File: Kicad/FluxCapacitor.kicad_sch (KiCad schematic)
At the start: 67 parts, among them J1 Jack-DC, J10 RELAY, J19 Conn_01x03_Socket, J2 TM_1, J20 Conn_01x03_Socket, J21 Conn_01x03_Socket, J22 Conn_01x03_Socket, J23 Conn_01x03_Socket, J3 TM_2, J4 Conn_01x02, J7 TM_1, J8 TM_1, J9 RELAY, K1 G5V-1, Q1 2N7000, Q2 IRF4905PBF, SW1 SW_SPDT_321, U1 OKI-78SR-5_1.5-W36-C, U2 ESP32_DEVBOARD

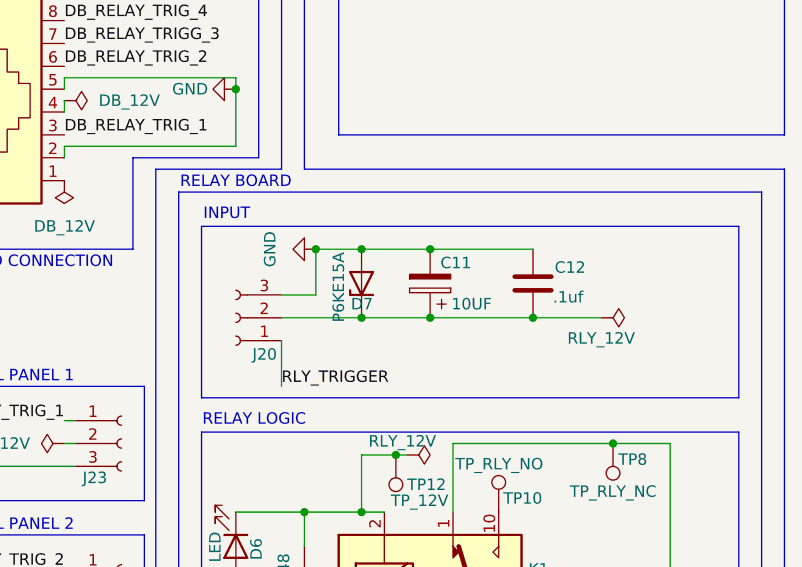
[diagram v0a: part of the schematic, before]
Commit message: File organization and power input work
-Changed file structure to make space for fusion files and firmware in one github repo.
-updated gitignore to account for fusion.
-added a mosfet for reverse polarity protection.
-changed electrolytic caps to polarized. -Created a flux capacitor library stored in the repo so that symbols aren't dependent on my personal library
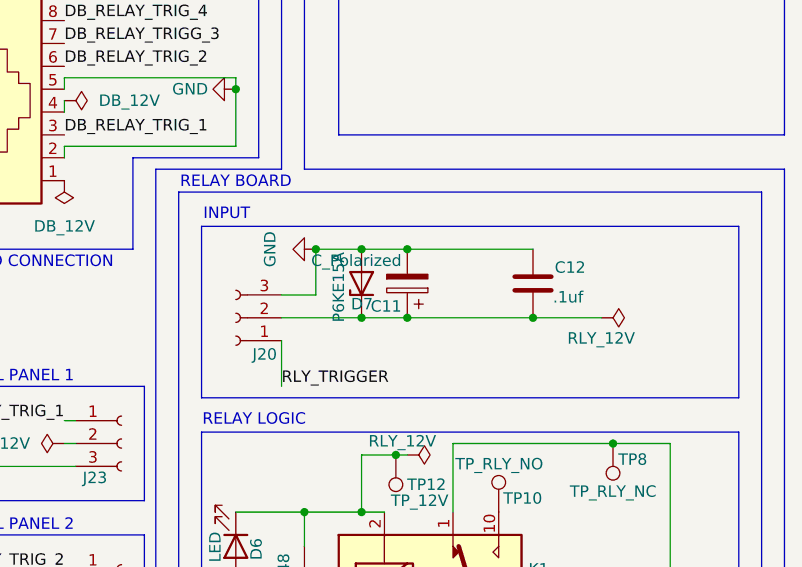
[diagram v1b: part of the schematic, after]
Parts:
- C11: value 10UF -> C_Polarized
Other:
- moved on the sheet: C11
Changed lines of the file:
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@@
 	)
 	(junction
-		(at 132.08 88.9)
+		(at 238.76 87.63)
 		(diameter 0)
 		(color 0 0 0 0)
 	)
 	(junction
-		(at 38.1 76.2)
+		(at 132.08 88.9)
 		(diameter 0)
 		(color 0 0 0 0)
 	)
 	(junction
-		(at 160.02 88.9)
+		(at 38.1 76.2)
 		(diameter 0)
 		(color 0 0 0 0)
 	)
 	(junction
-		(at 25.4 177.8)
+		(at 160.02 88.9)
 		(diameter 0)
 		(color 0 0 0 0)
 	)
 	(junction
-		(at 241.3 87.63)
+		(at 25.4 177.8)
 		(diameter 0)
 		(color 0 0 0 0)
@@
 	)
 	(junction
-		(at 241.3 80.01)
-		(diameter 0)
-		(color 0 0 0 0)
-	)
-	(junction
 		(at 137.16 76.2)
 		(diameter 0)
@@
 	)
 	(junction
+		(at 238.76 80.01)
+		(diameter 0)
+		(color 0 0 0 0)
+	)
+	(junction
 		(at 236.22 133.35)
 		(diameter 0)
@@
 	(wire
 		(pts
-			(xy 241.3 87.63) (xy 252.73 87.63)
-		)
-		(stroke
-			(width 0)
-			(type default)
-		)
-	)
-	(wire
-		(pts
 			(xy 114.3 151.13) (xy 114.3 171.45)
 		)
@@
 	(wire
 		(pts
-			(xy 233.68 80.01) (xy 241.3 80.01)
+			(xy 233.68 80.01) (xy 238.76 80.01)
 		)
 		(stroke
@@
 	(wire
 		(pts
-			(xy 233.68 87.63) (xy 241.3 87.63)
+			(xy 233.68 87.63) (xy 238.76 87.63)
 		)
 		(stroke
@@
 	(wire
 		(pts
+			(xy 238.76 80.01) (xy 252.73 80.01)
+		)
+		(stroke
+			(width 0)
+			(type default)
+		)
+	)
+	(wire
+		(pts
 			(xy 132.08 96.52) (xy 132.08 97.79)
 		)
@@
 	(wire
 		(pts
+			(xy 238.76 87.63) (xy 252.73 87.63)
+		)
+		(stroke
+			(width 0)
+			(type default)
+		)
+	)
+	(wire
+		(pts
 			(xy 137.16 168.91) (xy 137.16 171.45)
 		)
@@
 	(wire
 		(pts
-			(xy 241.3 80.01) (xy 252.73 80.01)
-		)
-		(stroke
-			(width 0)
-			(type default)
-		)
-	)
-	(wire
-		(pts
 			(xy 40.64 69.85) (xy 40.64 68.58)
 		)
@@
 	(symbol
 		(lib_id "Device:C_Polarized")
-		(at 241.3 83.82 180)
+		(at 238.76 83.82 180)
 		(unit 1)
 		(body_style 1)
@@
 		(dnp no)
 		(property "Reference" "C11"
-			(at 245.872 81.534 0)
+			(at 238.125 86.36 0)
 			(show_name no)
 			(do_not_autoplace no)
@@
 			)
 		)
-		(property "Value" "10UF"
-			(at 248.158 86.106 0)
+		(property "Value" "C_Polarized"
+			(at 238.125 81.28 0)
 			(show_name no)
 			(do_not_autoplace no)
@@
 		)
 		(property "Footprint" ""
-			(at 240.3348 80.01 0)
+			(at 237.7948 80.01 0)
 			(hide yes)
 			(show_name no)
@@
 		)
 		(property "Datasheet" ""
-			(at 241.3 83.82 0)
+			(at 238.76 83.82 0)
 			(hide yes)
 			(show_name no)
@@
 		)
 		(property "Description" "Polarized capacitor"
-			(at 241.3 83.82 0)
+			(at 238.76 83.82 0)
 			(hide yes)
 			(show_name no)

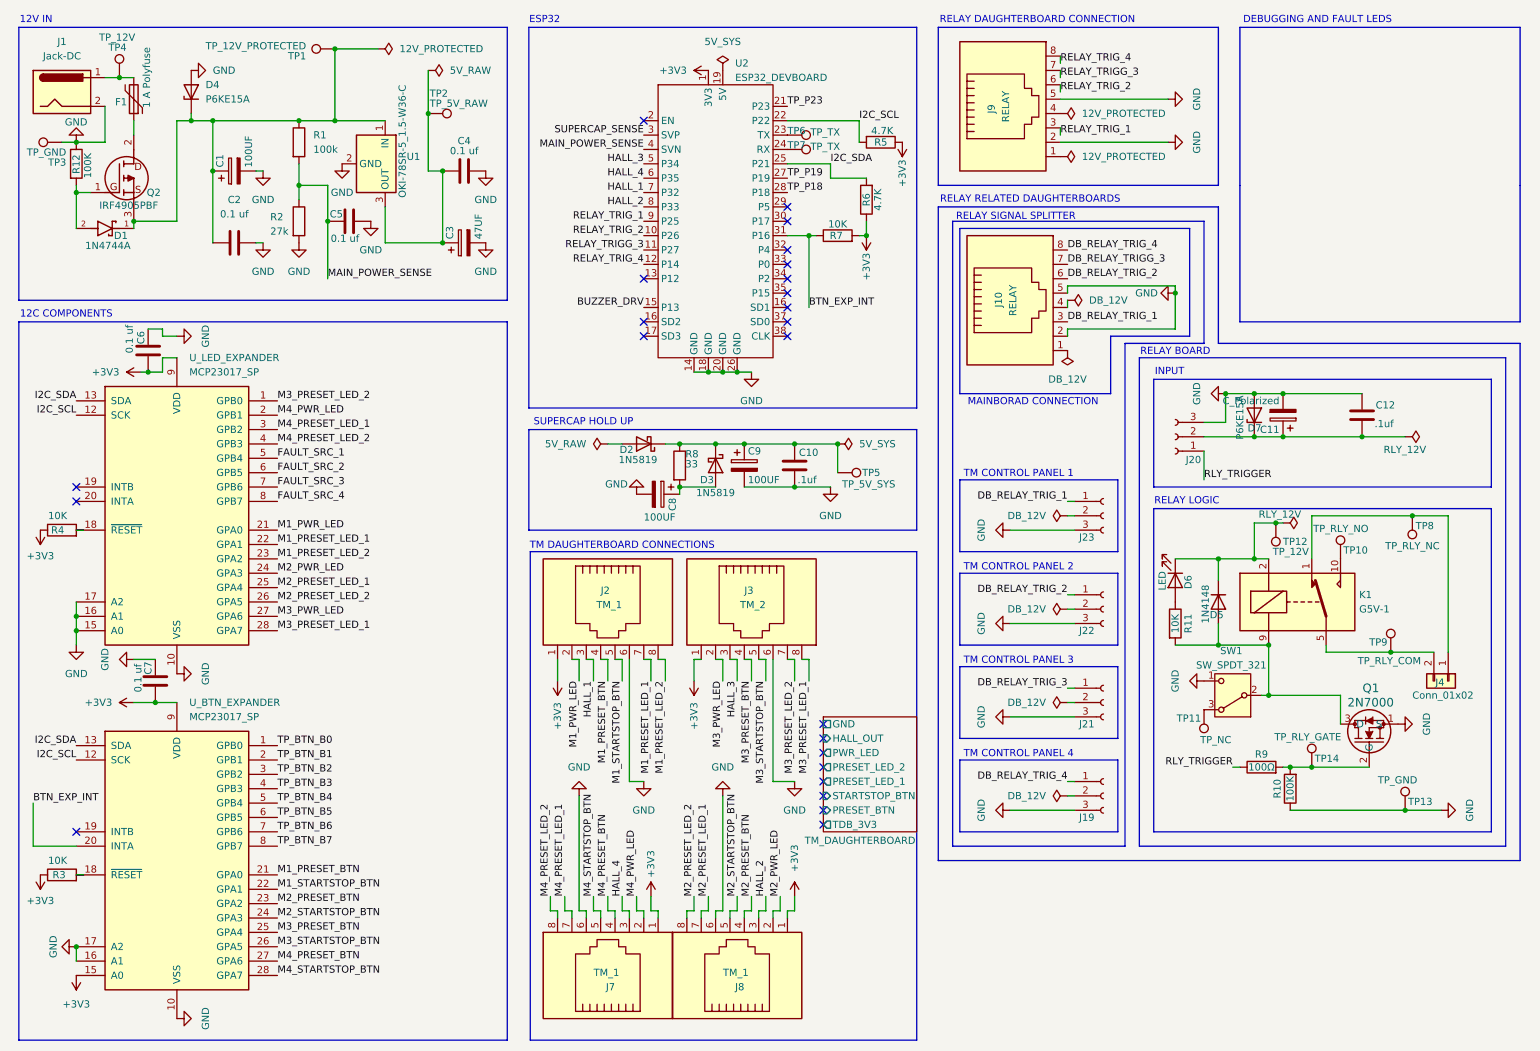
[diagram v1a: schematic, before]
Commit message: Finished Schematic
   did
-All debugging leds
-buzzer
-ran ERC

to do
-fix ERC problems

it is
-too late lol
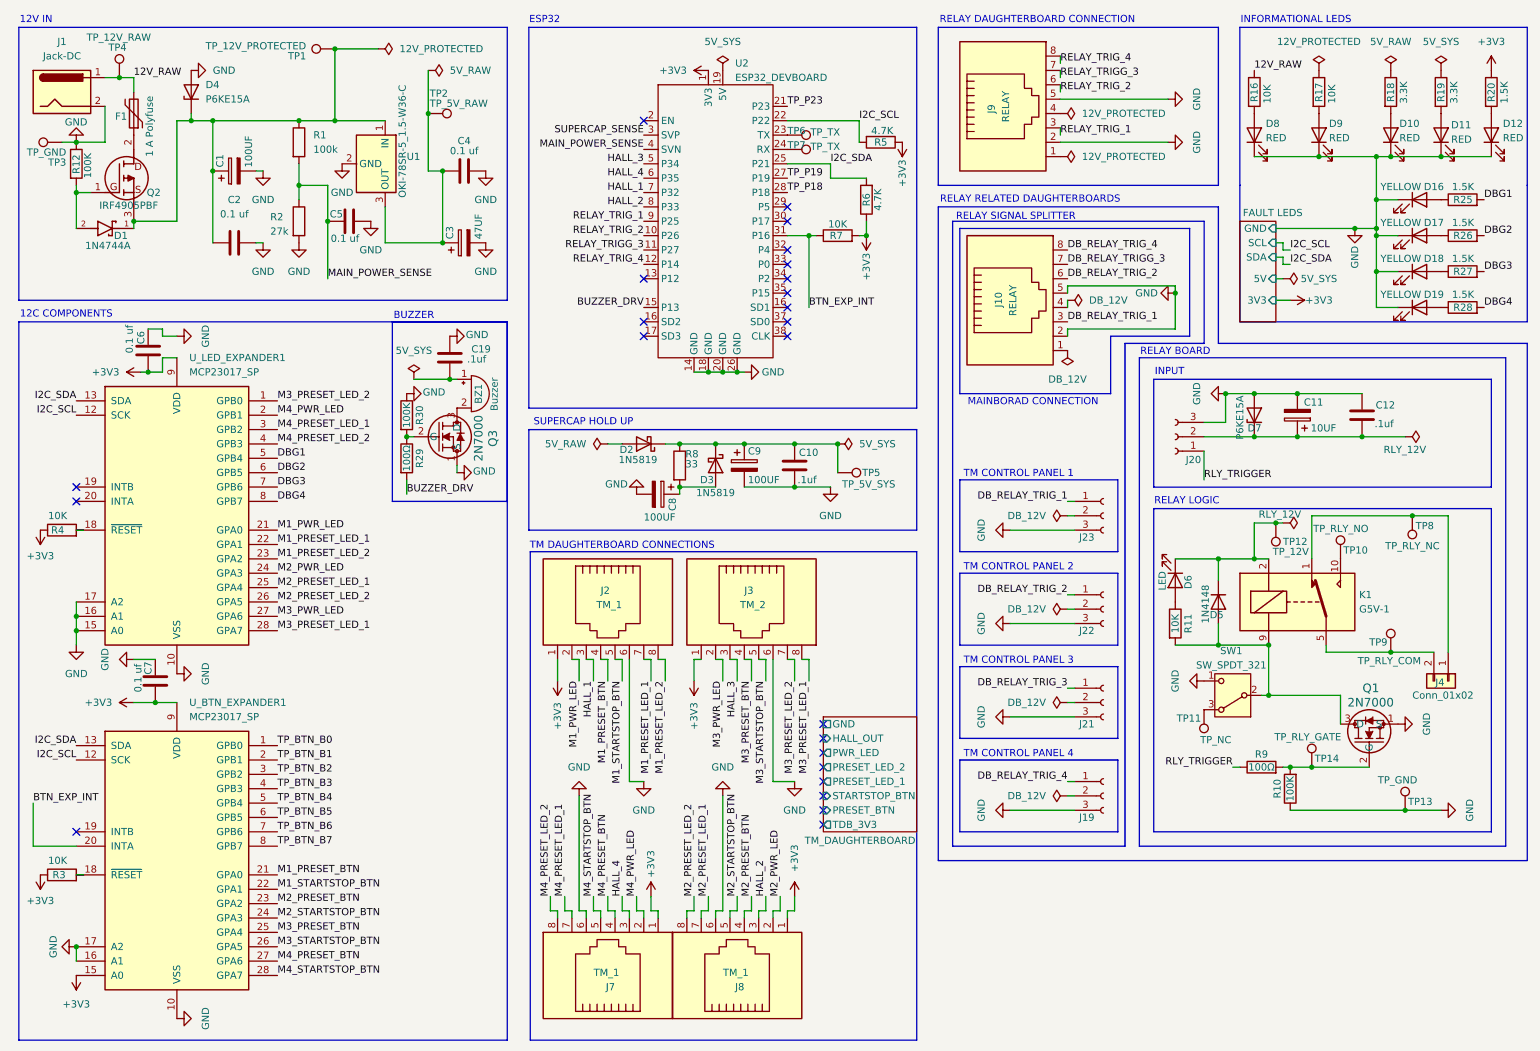
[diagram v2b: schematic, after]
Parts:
- added BZ1: Buzzer, symbol Device:Buzzer
- added C19: .1uf, symbol Device:C
- added D10, D11, D12, D8, D9: RED, symbol Device:LED
- added D16, D17, D18, D19: YELLOW, symbol Device:LED
- added Q3: 2N7000, Q_TO-92_135AN_OSI, symbol Generic:2N7000
- added R16, R17: 10K, symbol Device:R
- added R18, R19: 3.3K, symbol Device:R
- added R20, R25, R26, R27, R28: 1.5K, symbol Device:R
- added R29: 100Ω, symbol Device:R
- added R30: 100K, symbol Device:R
- C11: value C_Polarized -> 10UF
- TP4: value TP_12V -> TP_12V_RAW
- renumbered U_BTN_EXPANDER to U_BTN_EXPANDER1, U_LED_EXPANDER to U_LED_EXPANDER1
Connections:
- net +3V3: now also R20.1
- net BUZZER_DRV: now also R29.2
- net GND: now also C19.1, D10.1 (K), D11.1 (K), D12.1 (K), D16.1 (K), D17.1 (K), D18.1 (K), D19.1 (K), D8.1 (K), D9.1 (K), Q3.1 (S), R30.1
- net 12V_RAW: now reaches F1.2, J1.1, TP4.1
- net 12V_RAW: now also R16.1
- net FAULT_SRC_1 renamed DBG1
- net DBG1: now also R25.2
- net FAULT_SRC_2 renamed DBG2
- net DBG2: now also R26.2
- net FAULT_SRC_3 renamed DBG3
- net DBG3: now also R27.2
- net FAULT_SRC_4 renamed DBG4
- net DBG4: now also R28.2
- new net: D9.2 (A), R17.2
- new net: D12.2 (A), R20.2
- new net: D10.2 (A), R18.2
- new net: D11.2 (A), R19.2
- new net: D17.2 (A), R26.1
- new net: D19.2 (A), R28.1
- new net: Q3.2 (G), R29.1, R30.2
- new net: BZ1.2 (-), Q3.3 (D)
- new net: D8.2 (A), R16.2
- new net: BZ1.1 (+), C19.2
- new net: D16.2 (A), R25.1
- new net: D18.2 (A), R27.1
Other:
- added sheet FAULT LEDS (FAULT_LEDS.kicad_sch)
- note added: "BUZZER"
- note added: "INFORMATIONAL LEDS"
- note removed: "DEBUGGING AND FAULT LEDS"
- moved on the sheet: C11, F1

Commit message: ADDED OPTIONAL FAN HEADER
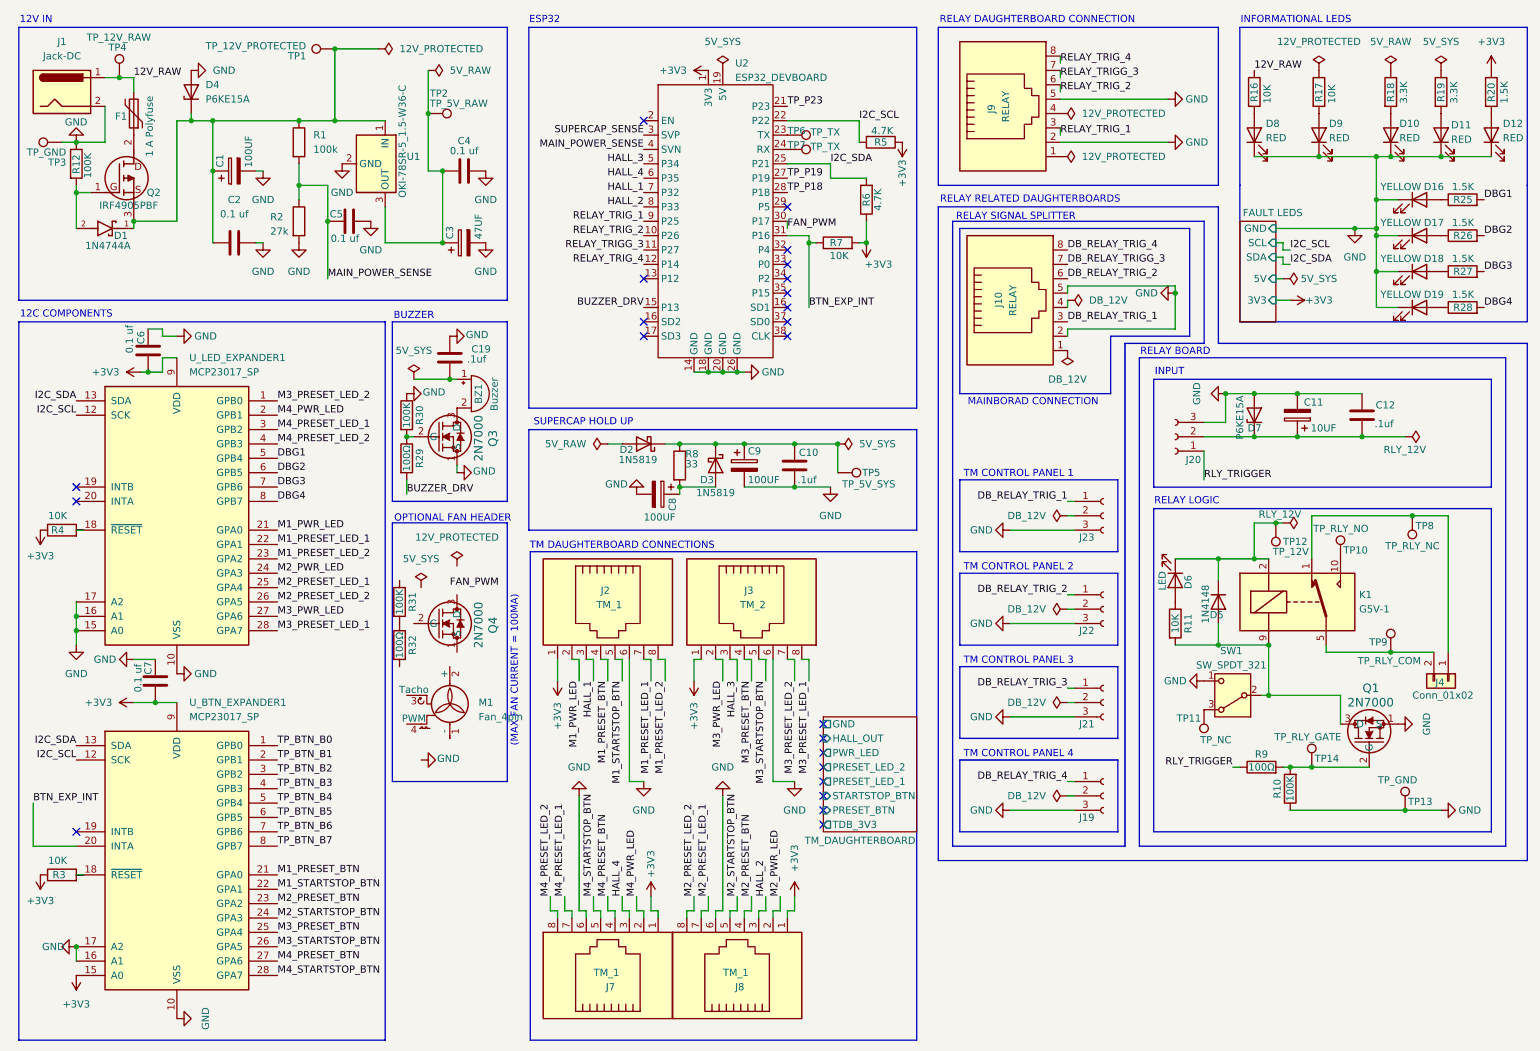
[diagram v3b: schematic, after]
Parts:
- added M1: Fan_4pin, symbol Motor:Fan_4pin
- added Q4: 2N7000, Q_TO-92_135AN_OSI, symbol Generic:2N7000
- added R31: 100K, symbol Device:R
- added R32: 100Ω, symbol Device:R
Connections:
- net FAN_PWM: now reaches U2.30 (P17)
- new net: R31.2, R32.1
- no-connect marks 24 -> 23
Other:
- note added: "(MAX FAN CURRENT = 100MA)"
- note added: "OPTIONAL FAN HEADER"
- moved on the sheet: R7
